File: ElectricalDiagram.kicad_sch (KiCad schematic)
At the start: 29 parts

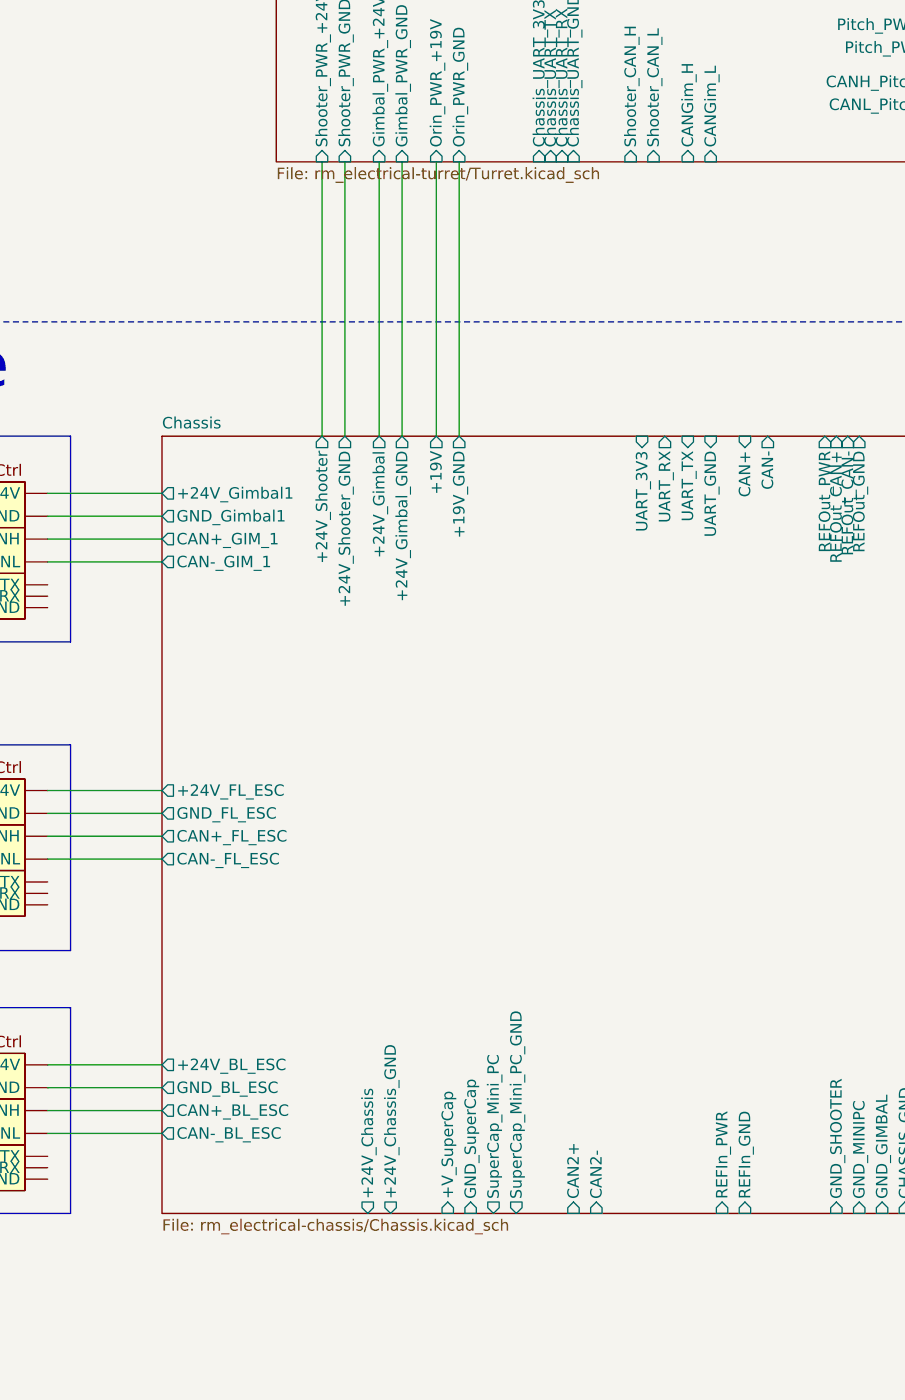
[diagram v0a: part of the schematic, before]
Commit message: update relative paths for subsheets
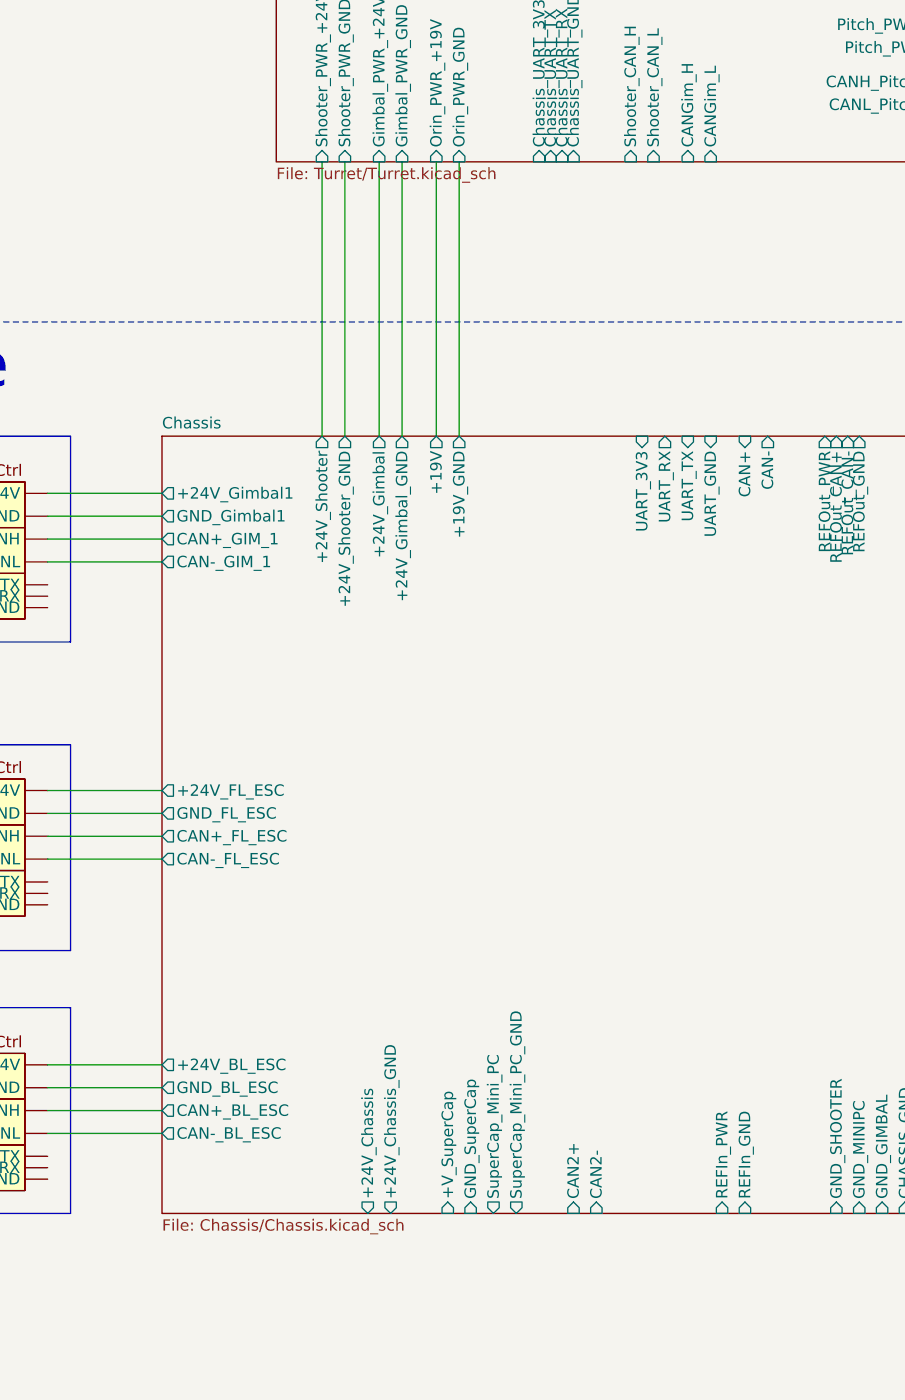
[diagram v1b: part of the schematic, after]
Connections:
- net at U27. (CANL): no longer U28. (GND)
- net at U3. (Ref_Out): now also U4. (Ref_Out)
- net at U4. (Ref_Out): no longer U3. (Ref_Out)
- new net: U10. (7-Pin), U12. (7-Pin) (x3)
- new net: U5. (7-Pin), U7. (7-Pin) (x3)
- new net: U11. (7-Pin), U13. (7-Pin) (x3)
- new net: U14. (7-Pin), U15. (7-Pin) (x3)
- new net: U24. (7-Pin), U25. (7-Pin) (x3)
- new net: U27. (CANL), U28. (GND)
- new net: U8. (7-Pin), U9. (7-Pin) (x3)
- new net: U22. (7-Pin), U23. (7-Pin) (x3)
- new net: U20. (7-Pin), U21. (7-Pin) (x3)
- new net: U16. (7-Pin), U17. (7-Pin) (x3)
- new net: U18. (7-Pin), U19. (7-Pin) (x3)
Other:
- sheet Chassis: file rm_electrical-chassis/Chassis.kicad_sch -> Chassis/Chassis.kicad_sch
- sheet Turret: file rm_electrical-turret/Turret.kicad_sch -> Turret/Turret.kicad_sch
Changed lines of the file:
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@@
 			)
 		)
-		(property "Sheetfile" "rm_electrical-chassis/Chassis.kicad_sch"
+		(property "Sheetfile" "Chassis/Chassis.kicad_sch"
 			(at 76.2 246.9646 0)
 			(effects
@@
 			)
 		)
-		(property "Sheetfile" "rm_electrical-turret/Turret.kicad_sch"
+		(property "Sheetfile" "Turret/Turret.kicad_sch"
 			(at 88.9 130.1246 0)
 			(effects
